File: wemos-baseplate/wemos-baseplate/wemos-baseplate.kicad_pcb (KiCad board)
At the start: 2 copper layers, 3 parts, among them U1 ESP32-MINI-32, U2 ESP32-MINI-32, U3 ESP32-MINI-32

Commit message: footprint OK
horizontal lines set
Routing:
- net /GND: track 2.75 -> 231.0 mm
- net /TMS: track 0.00 -> 115.4 mm
- net /SD2: track 0.00 -> 115.4 mm
- net /IO33: track 0.00 -> 115.4 mm
- net /NC1: track 0.00 -> 115.4 mm
- net /SVN: track 0.00 -> 115.4 mm
- net /NC2: track 0.00 -> 115.4 mm
- net /IO35: track 0.00 -> 115.4 mm
- net /IO34: track 0.00 -> 115.4 mm
- net /CMD: track 0.00 -> 115.4 mm
- net /TDO: track 0.00 -> 76.7 mm
- net /IO17: track 0.00 -> 76.7 mm
- net /TXD: track 0.00 -> 76.7 mm
- net /RST: track 0.00 -> 76.7 mm
- net /IO23: track 0.00 -> 76.7 mm
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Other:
- net class Power added: clearance 0.2, trace_width 0.25, via_dia 0.8, via_drill 0.4

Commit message: corrected lib
added spreadsheet with PinMapping
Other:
- copper layers 2 -> 4

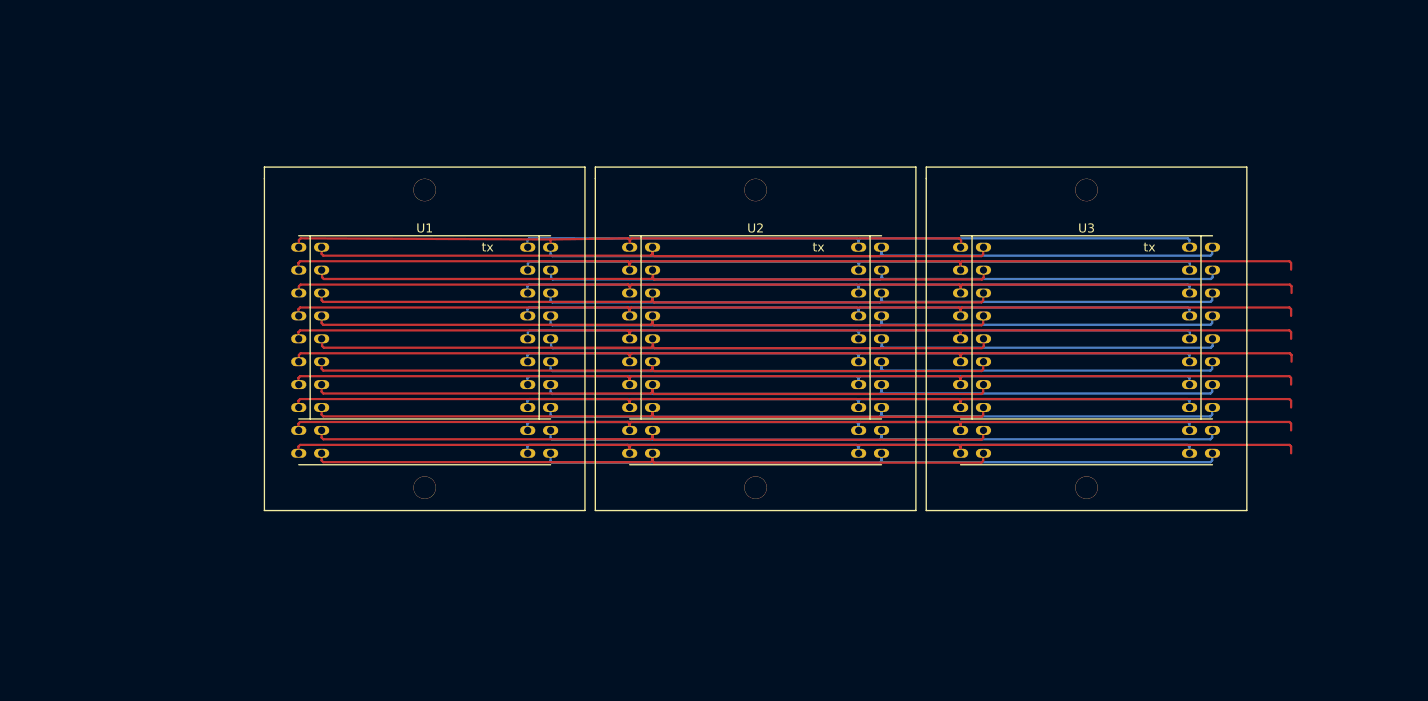
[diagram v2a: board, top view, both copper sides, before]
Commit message: 1st print layout with i2c/grove and extention connectors
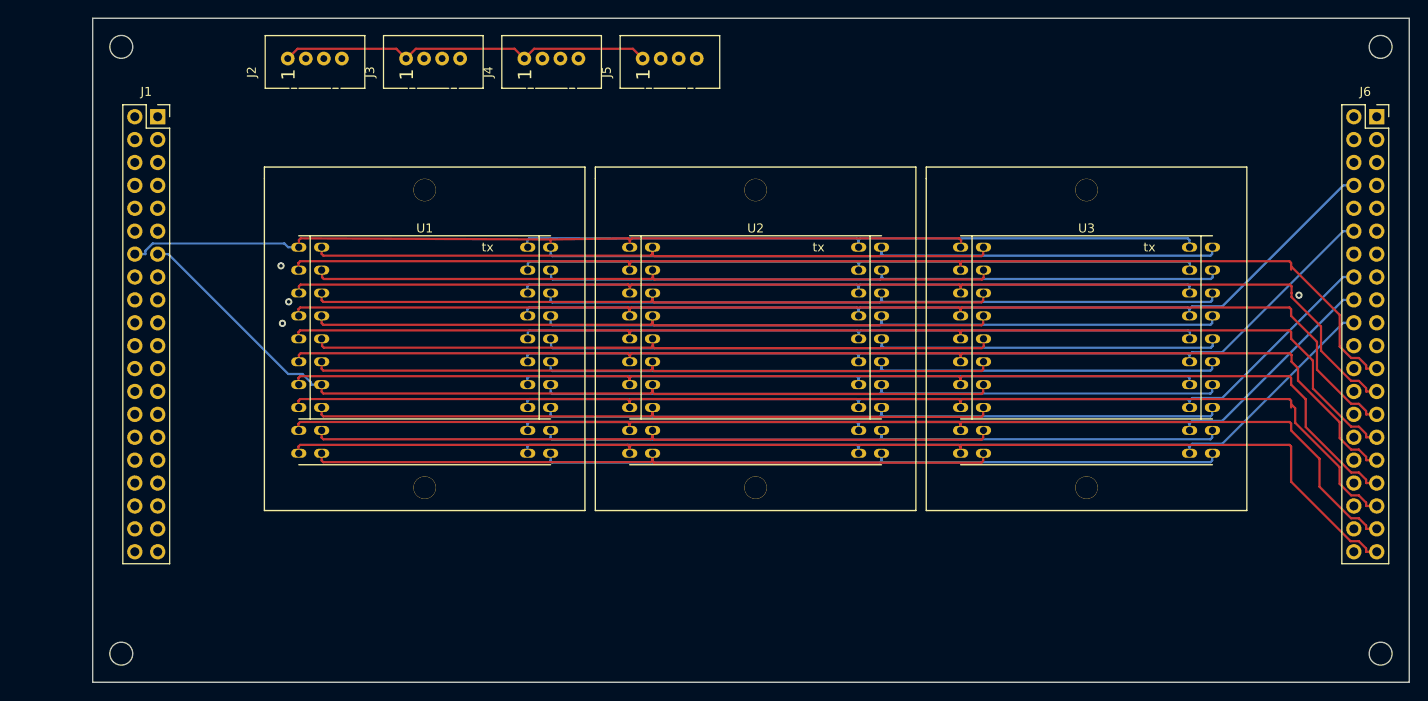
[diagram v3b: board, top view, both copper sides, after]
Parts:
- added J1: Conn_02x20_Odd_Even, Connector_PinSocket_2.54mm:PinSocket_2x20_P2.54mm_Vertical, F.Cu at (78.3, 82.0)
- added J2: Conn_01x04, Connectors:Grove_1x04, F.Cu at (92.8, 75.6)
- added J3: Conn_01x04, Connectors:Grove_1x04, F.Cu at (105.9, 75.6)
- added J4: Conn_01x04, Connectors:Grove_1x04, F.Cu at (119.0, 75.6)
- added J5: Conn_01x04, Connectors:Grove_1x04, F.Cu at (132.1, 75.6)
- added J6: Conn_02x20_Odd_Even, Connector_PinSocket_2.54mm:PinSocket_2x20_P2.54mm_Vertical, F.Cu at (213.6, 82.0)
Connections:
- net /3.3V renamed +3V3
- net /5V renamed +5C
- net /GND renamed GNDPWR
- net /IO21 renamed /SDA
- net /IO22 renamed /SCL
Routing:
- net +3V3: track 76.7 -> 233.4 mm
- net GNDPWR: track 231.0 -> 379.1 mm
- net /SDA: track 76.7 -> 202.9 mm
- net /SCL: track 76.7 -> 200.0 mm
- net /IO19: track 76.7 -> 155.9 mm
- net /IO17: track 76.7 -> 154.7 mm, vias 0 -> 1
- net /IO02: track 76.7 -> 152.6 mm
- net /TXD: track 76.7 -> 152.3 mm
- net /SDO: track 76.7 -> 152.1 mm
- net +5C: track 76.7 -> 152.1 mm
- net /IO16: track 76.7 -> 152.1 mm
- net /TDO: track 76.7 -> 152.1 mm
- net /RXD: track 76.7 -> 152.1 mm
- net /SVP: track 76.7 -> 151.9 mm
- net /IO18: track 76.7 -> 151.4 mm
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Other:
- board outline added: 146 x 73.7 mm

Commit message: versie met 30 pinnen in connector
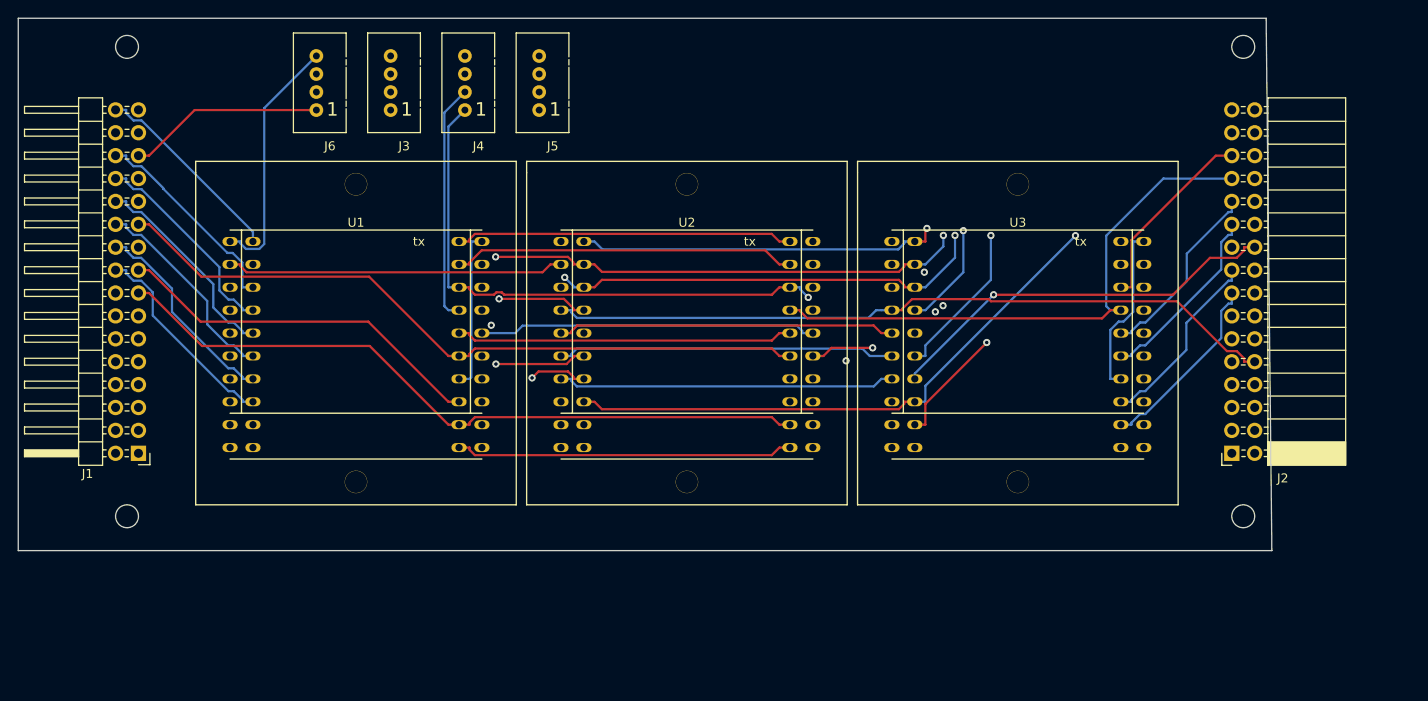
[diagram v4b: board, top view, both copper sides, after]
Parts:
- J1: value Conn_02x20_Odd_Even -> Conn_02x16_Odd_Even; footprint Connector_PinSocket_2.54mm:PinSocket_2x20_P2.54mm_Vertical -> Connector_PinHeader_2.54mm:PinHeader_2x16_P2.54mm_Horizontal
- J2: value Conn_01x04 -> Conn_02x16_Odd_Even; footprint Connectors:Grove_1x04 -> Connector_PinSocket_2.54mm:PinSocket_2x16_P2.54mm_Horizontal
- J6: value Conn_02x20_Odd_Even -> Conn_01x04; footprint Connector_PinSocket_2.54mm:PinSocket_2x20_P2.54mm_Vertical -> Connectors:Grove_1x04
- moved J6 117.6 mm to (95.9, 81.3), turned to 180 degrees
- moved J2 113.5 mm to (197.5, 119.4), turned to 180 degrees
- moved J1 37.4 mm to (76.2, 119.4), turned to 180 degrees
- moved J5 12.8 mm to (120.7, 81.3), turned to 180 degrees
- moved J4 8.73 mm to (112.4, 81.3), turned to 180 degrees
- moved U1 7.65 mm to (100.3, 106.0)
- moved U2 7.65 mm to (137.0, 106.0)
- moved U3 7.65 mm to (173.8, 106.0)
- moved J3 5.97 mm to (104.2, 81.3), turned to 180 degrees
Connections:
- J1 pad 1: /RST -> /IO02
- J1 pad 10: /IO17 -> /IO35
- J1 pad 11: /IO23 -> /IO25
- J1 pad 12: /IO16 -> /SVN
- J1 pad 13: /IO05 -> /IO27
- J1 pad 14: GNDPWR -> /NC1
- J1 pad 15: +3V3 -> /TDO
- J1 pad 16: +5C -> /TCK
- J1 pad 17: /TCK -> +5C
- J1 pad 18: /TDO -> +3V3
- J1 pad 19: /SD3 -> GNDPWR
- J1 pad 2: /TXD -> /NC2
- J1 pad 20: /SDO -> /IO05
- J1 pad 21: GNDPWR -> /IO16
- J1 pad 22: GNDPWR -> /IO23
- J1 pad 23: /NC1 -> /IO17
- J1 pad 24: /IO27 -> /IO19
- J1 pad 25: /SVN -> /SDA
- J1 pad 26: /IO25 -> /IO18
- J1 pad 27: /IO35 -> /SCL
- J1 pad 28: /IO32 -> /IO26
- J1 pad 29: /IO33 -> /RXD
- J1 pad 3: /SVP -> /IO00
- J1 pad 30: /TDI -> /SVP
- J1 pad 31: /IO34 -> /TXD
- J1 pad 32: /IO04 -> /RST
- J1 pad 4: /RXD -> /TMS
- J1 pad 5: /IO26 -> /IO04
- J1 pad 6: /SCL -> /IO34
- J1 pad 7: /IO18 -> /TDI
- J1 pad 8: /SDA -> /IO33
- J1 pad 9: /IO19 -> /IO32
- J2 pad 1: /SCL -> /IO02
- J2 pad 2: /SDA -> /NC2
- J2 pad 3: +3V3 -> /IO00
- J2 pad 4: GNDPWR -> /TMS
- J6 pad 1: /RST -> /SCL
- J6 pad 2: /TXD -> /SDA
- J6 pad 3: /SVP -> +3V3
- J6 pad 4: /RXD -> GNDPWR
- U1 pad 11: /SDO -> /SD0
- U1 pad 32: /SDI -> /SD1
- U2 pad 11: /SDO -> /SD0
- U2 pad 32: /SDI -> /SD1
- U3 pad 11: /SDO -> /SD0
- U3 pad 32: /SDI -> /SD1
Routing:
- net /SDO: track 152.1 -> 0.00 mm
- net /SDI: track 150.0 -> 0.00 mm
- net GNDPWR: track 379.1 -> 237.3 mm
- net /CMD: track 152.6 -> 75.0 mm
- net /SD3: track 151.1 -> 75.1 mm
- net /SD2: track 152.6 -> 76.7 mm
- net /SD1: track 0.00 -> 75.1 mm
- net /SD0: track 0.00 -> 75.0 mm
- net /CLK: track 148.4 -> 75.1 mm
- net /SCL: track 200.0 -> 165.1 mm, vias 0 -> 1
- net +3V3: track 233.4 -> 209.7 mm, vias 0 -> 1
- net /IO02: track 152.6 -> 129.3 mm
- net /IO27: track 150.7 -> 127.9 mm, vias 1 -> 0
- net /IO00: track 150.3 -> 128.6 mm
- net /IO32: track 149.6 -> 128.2 mm, vias 1 -> 0
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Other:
- board size 146 x 73.7 mm -> 139.1 x 59.1 mm

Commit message: added grove connectors
added labels for grove connectors
added filled area's for ground and 3v3 plane
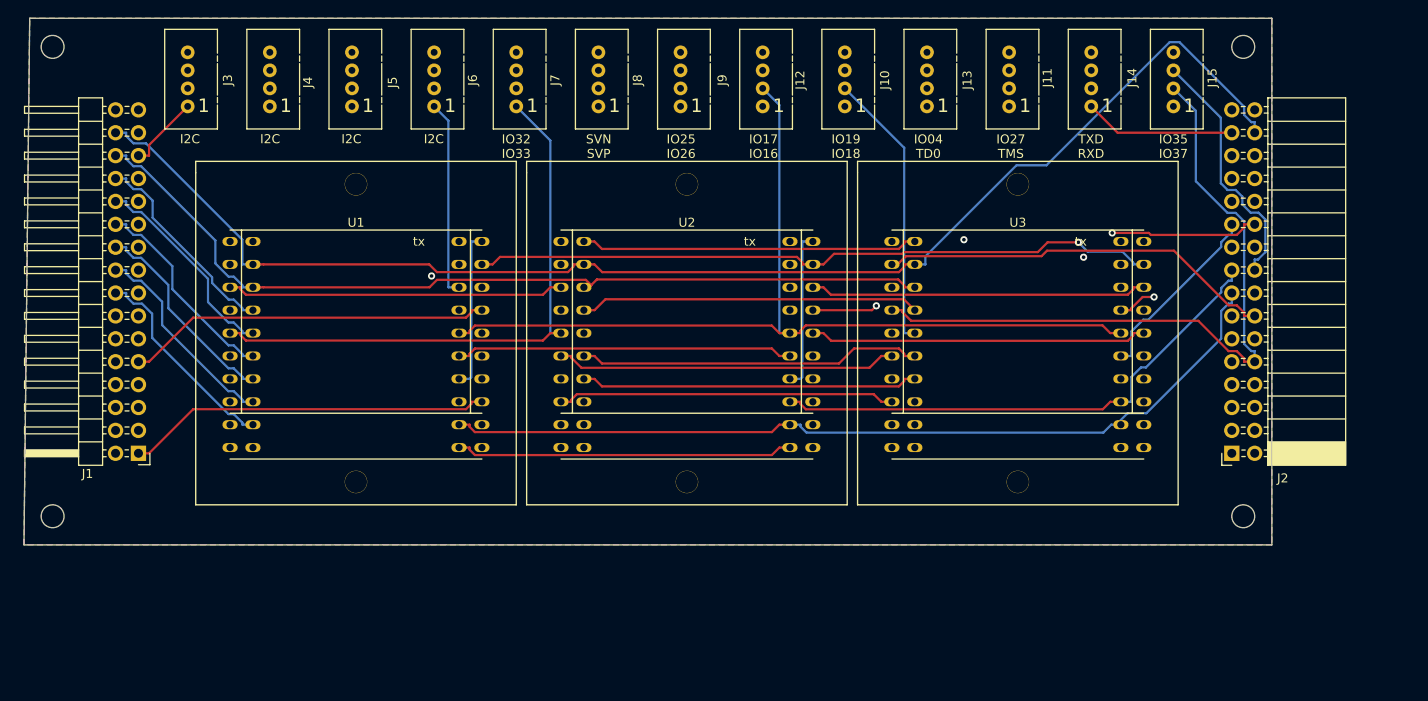
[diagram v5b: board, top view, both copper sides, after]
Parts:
- added J10: Conn_01x04, Connectors:Grove_1x04, F.Cu at (154.6, 80.9)
- added J11: Conn_01x04, Connectors:Grove_1x04, F.Cu at (172.8, 80.9)
- added J12: Conn_01x04, Connectors:Grove_1x04, F.Cu at (145.4, 80.9)
- added J13: Conn_01x04, Connectors:Grove_1x04, F.Cu at (163.7, 80.9)
- added J14: Conn_01x04, Connectors:Grove_1x04, F.Cu at (181.9, 80.9)
- added J15: Conn_01x04, Connectors:Grove_1x04, F.Cu at (191.0, 80.9)
- added J7: Conn_01x04, Connectors:Grove_1x04, F.Cu at (118.1, 80.9)
- added J8: Conn_01x04, Connectors:Grove_1x04, F.Cu at (127.2, 80.9)
- added J9: Conn_01x04, Connectors:Grove_1x04, F.Cu at (136.3, 80.9)
- moved J3 22.5 mm to (81.7, 80.9)
- moved J4 21.6 mm to (90.8, 80.9)
- moved J5 20.8 mm to (99.9, 80.9)
- moved J6 13.1 mm to (109.0, 80.9)
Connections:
- net +3V3 renamed /3.3V
- net +5C renamed /5V
- net /TDO renamed /TD0
- net GNDPWR renamed /GND
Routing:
- net /IO19: track 143.3 -> 201.9 mm, vias 1 -> 0
- net /GND: track 237.3 -> 295.0 mm
- net /IO34: track 134.3 -> 191.0 mm
- net /TD0: track 137.7 -> 193.3 mm
- net /3.3V: track 209.7 -> 261.9 mm, vias 1 -> 0
- net /IO25: track 128.4 -> 169.4 mm, vias 1 -> 0
- net /TMS: track 133.7 -> 169.8 mm
- net /IO04: track 128.3 -> 163.7 mm, vias 1 -> 0
- net /IO18: track 151.9 -> 186.3 mm, vias 2 -> 0
- net /IO35: track 134.3 -> 168.2 mm
- net /IO16: track 137.9 -> 171.0 mm, vias 1 -> 0
- net /SVP: track 143.0 -> 171.0 mm, vias 2 -> 0
- net /IO33: track 134.4 -> 160.9 mm
- net /5V: track 137.7 -> 163.9 mm
- net /IO17: track 143.2 -> 168.7 mm
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- added copper zone on F.Cu, net /3.3V
- added copper zone on B.Cu, net /GND
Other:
- board size 139.1 x 59.1 mm -> 138.4 x 58.4 mm
- net class Power: clearance 0.2 -> 0.25; trace_width 0.25 -> 0.3
- board text added: "I2C"
- board text added: "IO04 TD0"
- board text added: "IO17 IO16"
- board text added: "IO19 IO18"
- board text added: "IO25 IO26"
- board text added: "IO27 TMS"
- board text added: "IO32 IO33"
- board text added: "IO35 IO37"
- board text added: "SVN SVP"
- board text added: "TXD RXD"
